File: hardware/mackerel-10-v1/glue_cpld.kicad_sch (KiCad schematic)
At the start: 20 parts, among them J1 Conn_02x05_Odd_Even, J12 Conn_02x04_Odd_Even, J13 Conn_02x04_Odd_Even, J15 Conn_02x04_Odd_Even, J16 Conn_02x04_Odd_Even, X1 50MHz

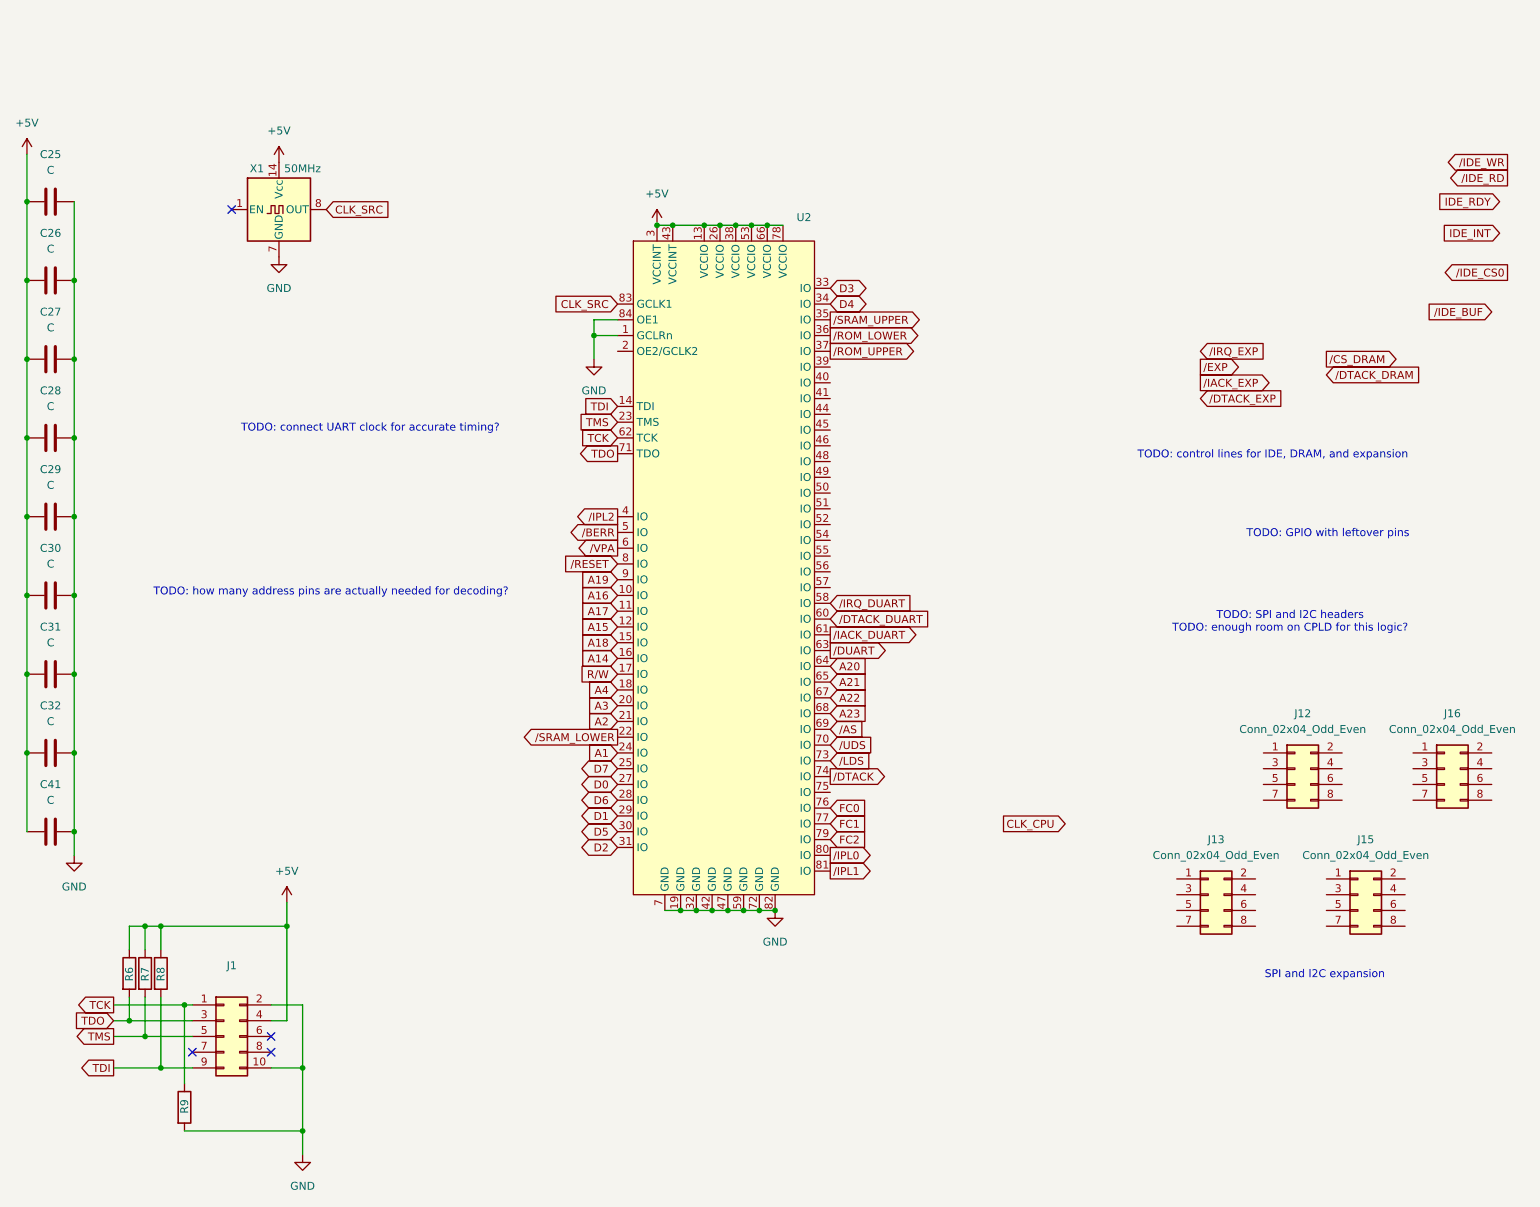
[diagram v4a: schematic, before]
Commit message: DRAM controller mostly routed
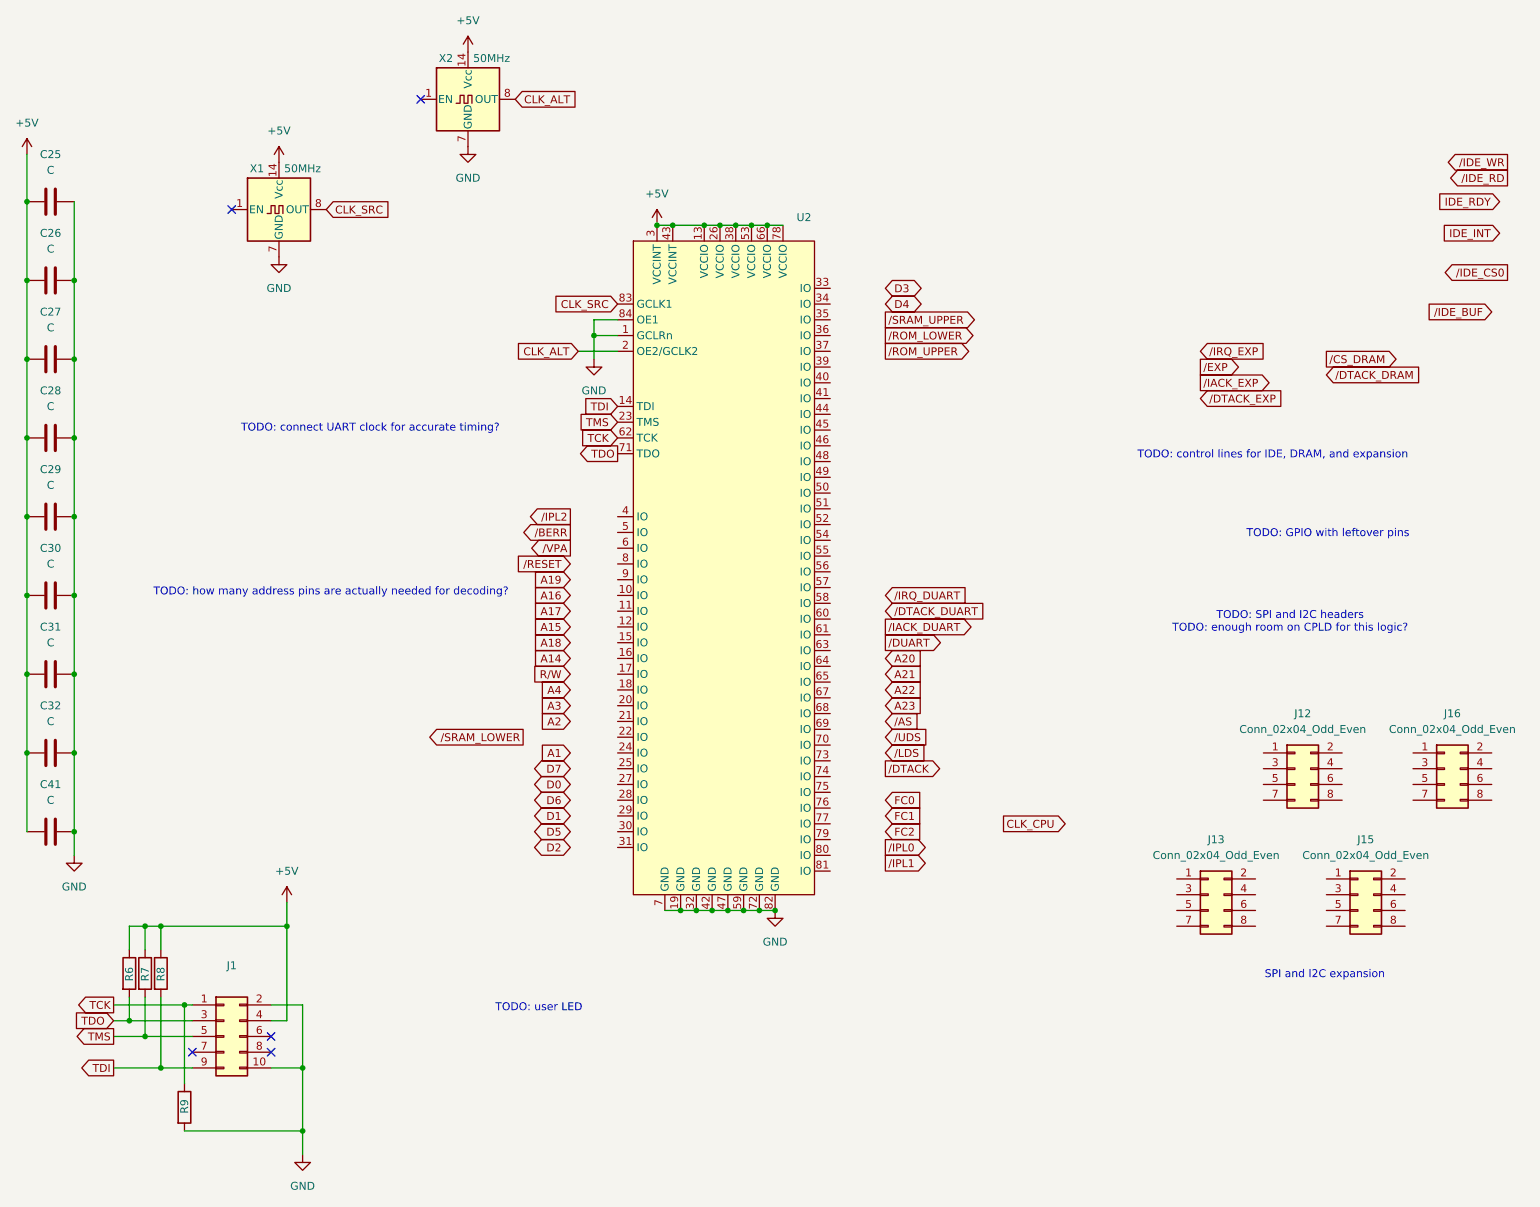
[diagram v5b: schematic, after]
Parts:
- added X2: 50MHz, Oscillator:Oscillator_DIP-14, symbol Oscillator:CXO_DIP14
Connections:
- net +5V: now also X2.14 (Vcc)
- net A1: no longer U2.24 (IO)
- net A14: no longer U2.16 (IO)
- net A15: no longer U2.12 (IO)
- net A16: no longer U2.10 (IO)
- net A17: no longer U2.11 (IO)
- net A18: no longer U2.15 (IO)
- net A19: no longer U2.9 (IO)
- net A2: no longer U2.21 (IO)
- net A20: no longer U2.64 (IO)
- net A21: no longer U2.65 (IO)
- net A22: no longer U2.67 (IO)
- net A23: no longer U2.68 (IO)
- net A3: no longer U2.20 (IO)
- net A4: no longer U2.18 (IO)
- net D0: no longer U2.27 (IO)
- net D1: no longer U2.29 (IO)
- net D2: no longer U2.31 (IO)
- net D3: no longer U2.33 (IO)
- net D4: no longer U2.34 (IO)
- net D5: no longer U2.30 (IO)
- net D6: no longer U2.28 (IO)
- net D7: no longer U2.25 (IO)
- net FC0: no longer U2.76 (IO)
- net FC1: no longer U2.77 (IO)
- net FC2: no longer U2.79 (IO)
- net GND: now also X2.7 (GND)
- net R/W: no longer U2.17 (IO)
- net /AS: no longer U2.69 (IO)
- net /BERR: no longer U2.5 (IO)
- net /DTACK: no longer U2.74 (IO)
- net /DTACK_DUART: no longer U2.60 (IO)
- net /DUART: no longer U2.63 (IO)
- net /IACK_DUART: no longer U2.61 (IO)
- net /IPL0: no longer U2.80 (IO)
- net /IPL1: no longer U2.81 (IO)
- net /IPL2: no longer U2.4 (IO)
- net /IRQ_DUART: no longer U2.58 (IO)
- net /LDS: no longer U2.73 (IO)
- net /RESET: no longer U2.8 (IO)
- net /ROM_LOWER: no longer U2.36 (IO)
- net /ROM_UPPER: no longer U2.37 (IO)
- net /SRAM_LOWER: no longer U2.22 (IO)
- net /SRAM_UPPER: no longer U2.35 (IO)
- net /UDS: no longer U2.70 (IO)
- net /VPA: no longer U2.6 (IO)
- net CLK_ALT: now reaches U2.2 (OE2/GCLK2)
- net CLK_ALT: now also X2.8 (OUT)
- no-connect marks 4 -> 5
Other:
- note added: "TODO: user LED"

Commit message: Glue logic CPLD almost fully routed
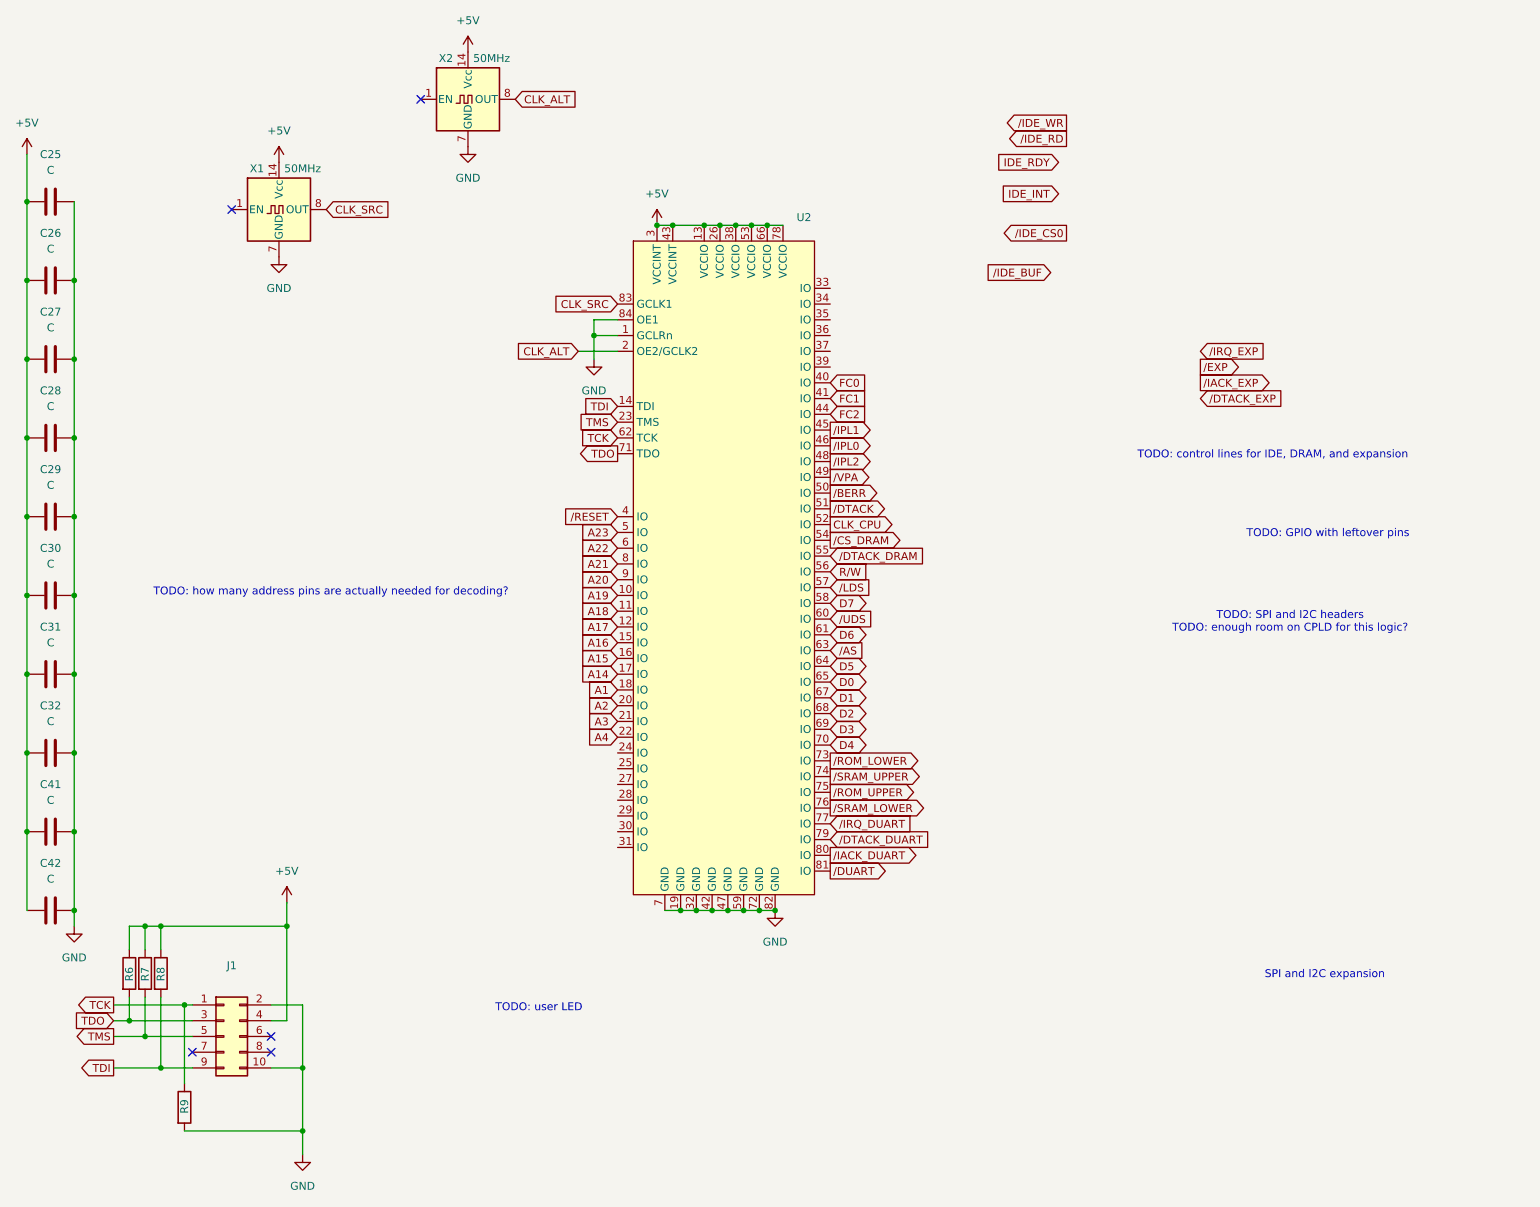
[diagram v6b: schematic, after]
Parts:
- removed J12, J13, J15, J16: Conn_02x04_Odd_Even, Connector_IDC:IDC-Header_2x04_P2.54mm_Vertical, symbol Connector_Generic:Conn_02x04_Odd_Even
- added C42: C, Capacitor_THT:C_Disc_D4.3mm_W1.9mm_P5.00mm, symbol Device:C
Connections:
- net +5V: now also C42.2
- net A1: now also U2.18 (IO)
- net A14: now also U2.17 (IO)
- net A15: now also U2.16 (IO)
- net A16: now also U2.15 (IO)
- net A17: now also U2.12 (IO)
- net A18: now also U2.11 (IO)
- net A19: now also U2.10 (IO)
- net A2: now also U2.20 (IO)
- net A20: now also U2.9 (IO)
- net A21: now also U2.8 (IO)
- net A22: now also U2.6 (IO)
- net A23: now also U2.5 (IO)
- net A3: now also U2.21 (IO)
- net A4: now also U2.22 (IO)
- net CLK_CPU: now also U2.52 (IO)
- net D0: now also U2.65 (IO)
- net D1: now also U2.67 (IO)
- net D2: now also U2.68 (IO)
- net D3: now also U2.69 (IO)
- net D4: now also U2.70 (IO)
- net D5: now also U2.64 (IO)
- net D6: now also U2.61 (IO)
- net D7: now also U2.58 (IO)
- net FC0: now also U2.40 (IO)
- net FC1: now also U2.41 (IO)
- net FC2: now also U2.44 (IO)
- net GND: now also C42.1
- net R/W: now also U2.56 (IO)
- net /AS: now also U2.63 (IO)
- net /BERR: now also U2.50 (IO)
- net /CS_DRAM: now also U2.54 (IO)
- net /DTACK: now also U2.51 (IO)
- net /DTACK_DRAM: now also U2.55 (IO)
- net /DTACK_DUART: now also U2.79 (IO)
- net /DUART: now also U2.81 (IO)
- net /IACK_DUART: now also U2.80 (IO)
- net /IPL0: now also U2.46 (IO)
- net /IPL1: now also U2.45 (IO)
- net /IPL2: now also U2.48 (IO)
- net /IRQ_DUART: now also U2.77 (IO)
- net /LDS: now also U2.57 (IO)
- net /RESET: now also U2.4 (IO)
- net /ROM_LOWER: now also U2.73 (IO)
- net /ROM_UPPER: now also U2.75 (IO)
- net /SRAM_LOWER: now also U2.76 (IO)
- net /SRAM_UPPER: now also U2.74 (IO)
- net /UDS: now also U2.60 (IO)
- net /VPA: now also U2.49 (IO)
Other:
- note removed: "TODO: connect UART clock for accurate timing?"

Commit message: Mostly routed except expansion
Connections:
- net /DTACK_DUART: now also U2.81 (IO); no longer U2.79 (IO)
- net /DUART: now also U2.79 (IO); no longer U2.81 (IO)
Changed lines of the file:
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@@
 	(global_label "{slash}DTACK_DUART"
 		(shape input)
-		(at 147.32 137.16 0)
-		(fields_autoplaced yes)
-		(effects
-			(font
-				(size 1.27 1.27)
-			)
-			(justify left)
-		)
-		(property "Intersheetrefs" "${INTERSHEET_REFS}"
-			(at 164.3962 137.16 0)
+		(at 147.32 142.24 0)
+		(fields_autoplaced yes)
+		(effects
+			(font
+				(size 1.27 1.27)
+			)
+			(justify left)
+		)
+		(property "Intersheetrefs" "${INTERSHEET_REFS}"
+			(at 164.3962 142.24 0)
 			(effects
 				(font
@@
 	(global_label "{slash}DUART"
 		(shape output)
-		(at 147.32 142.24 0)
-		(fields_autoplaced yes)
-		(effects
-			(font
-				(size 1.27 1.27)
-			)
-			(justify left)
-		)
-		(property "Intersheetrefs" "${INTERSHEET_REFS}"
-			(at 157.5624 142.24 0)
-			(effects
-				(font
+		(at 147.32 137.16 0)
+		(fields_autoplaced yes)
+		(effects
+			(font
+				(size 1.27 1.27)
+			)
+			(justify left)
+		)
+		(property "Intersheetrefs" "${INTERSHEET_REFS}"
+			(at 157.5624 137.16 0)
+			(effects
+				(font
